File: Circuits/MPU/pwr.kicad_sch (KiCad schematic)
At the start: 0 parts

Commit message: more transcription
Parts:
- added 	U1: ProASIC, Package_BGA:BGA-484_23.0x23.0mm_Layout22x22_P1.0mm, symbol QuERI_FPGA:ProASIC
- added C100, C101, C102, C103, C104, C105, C106, C99: 22nF, Capacitor_SMD:C_0603_1608Metric, symbol QuERI_symbols:Csmall
- added C107, C108, C109, C110, C111: 0.1uF, Capacitor_SMD:C_0805_2012Metric, symbol QuERI_symbols:C
- added C112, C113: 0.1uF, Capacitor_SMD:C_0603_1608Metric, symbol QuERI_symbols:Csmall
- added C114: 10uF, Capacitor_SMD:C_0805_2012Metric, symbol QuERI_symbols:C
- added C115, C116, C80: DNP, Capacitor_SMD:C_1210_3225Metric, symbol QuERI_symbols:C
- added C117, C79: 10uF, Capacitor_SMD:C_1210_3225Metric, symbol QuERI_symbols:C
- added C118, C120, C121, C123, C124, C129, C130, C131, C132: 1uF, Capacitor_SMD:C_0805_2012Metric, symbol QuERI_symbols:C
- added C119, C122: 7.5nF, Capacitor_SMD:C_0603_1608Metric, symbol QuERI_symbols:Csmall
- added C125, C127: 10nF, Capacitor_SMD:C_0603_1608Metric, symbol QuERI_symbols:Csmall
- added C126, C128: 47uF, Capacitor_SMD:C_1210_3225Metric, symbol QuERI_symbols:C
- added C73, C76, C78: 22uF, Capacitor_SMD:C_1210_3225Metric, symbol QuERI_symbols:C
- added C74, C75, C77: TBD, Capacitor_SMD:C_1210_3225Metric, symbol QuERI_symbols:C
- added D10, D11, D12, D13, D14, D15, D16, D17, D18, D19, D20, D21, D9: 1N914UR, Diode_SMD:D_MiniMELF, symbol QuERI_symbols:1N914UR
- added L1, L2, L3, L4, L7: 4.7uH, Inductor_SMD:L_1008_2520Metric, symbol Device:L
- added PS1: JCA0624S03, symbol QuERI_symbols:JCA0624S03
- added PS2: JCE0324D05, symbol QuERI_symbols:JCE0324D05
- added Q7, Q8: MMBT2222A, Package_TO_SOT_SMD:SOT-23, symbol Transistor_BJT:MMBT2222A
- added R155, R156, R157, R158, R159, R160: 169, Resistor_SMD:R_1206_3216Metric, symbol Device:R
- added R161, R163: 4.99k, Resistor_SMD:R_0603_1608Metric, symbol QuERI_symbols:Rlowp
- added R162, R180: 49.9, Resistor_SMD:R_0603_1608Metric, symbol QuERI_symbols:Rlowp
- added R164, R167: 3.01k, Resistor_SMD:R_0603_1608Metric, symbol QuERI_symbols:Rlowp
- added R165, R166, R171, R178: 1, Resistor_SMD:R_0603_1608Metric, symbol QuERI_symbols:Rlowp
- added R168, R173: 3.74k, Resistor_SMD:R_0603_1608Metric, symbol QuERI_symbols:Rlowp
- added R169, R174: 15.0k, Resistor_SMD:R_0603_1608Metric, symbol QuERI_symbols:Rlowp
- added R170: 1.87k, Resistor_SMD:R_0603_1608Metric, symbol QuERI_symbols:Rlowp
- added R172, R176, R177: 18.2k, Resistor_SMD:R_0603_1608Metric, symbol QuERI_symbols:Rlowp
- added R175, R179, R181: 4.99, Resistor_SMD:R_0603_1608Metric, symbol QuERI_symbols:Rlowp
- added T1: HPH1-1400L, symbol QuERI_symbols:Hexapath
- added U26: DG403, Package_SO:SOIC-16_3.9x9.9mm_P1.27mm, symbol QuERI_symbols:DG403
- added U27: REF43GS, Package_SO:SOIC-8_3.9x4.9mm_P1.27mm, symbol QuERI_symbols:REF43GS
- added U28, U29: ADA4805-2ARMZ, Package_SO:MSOP-8_3x3mm_P0.65mm, symbol QuERI_symbols:ADA4805-2ARMZ
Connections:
- net +3.3raw: now also C74.1, L1.1, PS1.14 (+Vout)
- net +5raw: now also C75.1, L2.1, PS2.14 (+Vout)
- net -5raw: now also C77.1, L3.1, PS2.11 (-Vout)
- new net: C107.1, C109.2, D10.2 (A), D11.1 (K)
- new net: C106.1, C108.2, D11.2 (A), D12.1 (K)
- new net: C112.1, R155.2, U26.11 (V+), U26.12 (VL)
- new net: C123.1, R168.2, R169.2, U28.5 (+)
- new net: R160.2, U26.9 (S2)
- new net: C131.1, R180.2, U29.8 (V+)
- new net: Q8.1 (B), U29.1
- new net: C127.2, R177.1, U29.2 (-)
- new net: R176.2, U29.3 (+)
- new net: C101.2, C99.1, D18.2 (A), D19.1 (K)
- new net: C105.1, C107.2, D12.2 (A), D13.1 (K)
- new net: C103.1, C105.2, D14.2 (A), D15.1 (K)
- new net: C119.2, R163.2, R164.1, U28.2 (-)
- new net: C104.1, C106.2, D13.2 (A), D14.1 (K)
- new net: C102.1, C104.2, D15.2 (A), D16.1 (K)
- new net: C118.1, R162.2, U27.2 (VIN)
- new net: C125.1, Q7.2 (E), R171.1
- new net: C125.2, R172.1, U29.6 (-)
- new net: R173.2, R174.2, U29.5 (+)
- new net: C117.1, C79.2, L7.2, PS1.2 (-Vin), PS1.3 (-Vin), PS2.2 (-Vin), PS2.3 (-Vin)
- new net: C117.2, C79.1, L4.2, PS1.22 (+Vin), PS1.23 (+Vin), PS2.22 (+Vin), PS2.23 (+Vin)
- new net: C101.1, C103.2, D16.2 (A), D17.1 (K)
- new net: C100.1, C102.2, D17.2 (A), D18.1 (K)
- new net: C108.1, C110.2, D10.1 (K), D9.2 (A)
- new net: C127.1, Q8.2 (E), R178.1
- new net: C132.1, R181.2, U28.8 (V+)
- new net: Q7.1 (B), U29.7
- new net: C129.1, Q8.3 (C), R179.2
- new net: R159.2, U26.5 (S4)
- new net: C110.1, T1.9
- new net: R158.2, U26.16 (S1)
- new net: C100.2, D19.2 (A), D20.1 (K)
- new net: C130.1, Q7.3 (C), R175.2
- new net: C119.1, R165.1, U28.1
- new net: C124.1, R170.2, U28.3 (+)
- new net: C111.1, U26.1 (D1), U26.3 (D3), U26.6 (D4), U26.8 (D2)
- new net: C111.2, T1.2, T1.6
- new net: 	U1.AB12 (PUR), C114.1, D21.2 (A), R161.2
- new net: 	U1.AB13 (HVCLK), U26.10 (IN2), U26.15 (IN1)
- new net: C122.2, R167.1, U28.6 (-)
- new net: C122.1, R166.1, U28.7
- new net: C113.1, R156.2, U26.14 (V-)
- new net: R157.2, U26.4 (S3)
- new net: T1.1, T1.5
- new net: T1.10, T1.3
- new net: T1.11, T1.7
- new net: T1.12, T1.8
- new net +1.5V: C126.1, R171.2, R172.2
- new net +2.5F: C128.1, R177.2, R178.2
- new net +2.5V: R168.1, R170.1, R173.1, R176.1, U27.6 (VOUT)
- new net +28V: C116.2, C80.1, L4.1
- new net +28return: C115.1, C80.2, L7.1
- new net +3.3V: C73.1, D21.1 (K), L1.2, R161.1, R175.1, R179.1
- new net +5V: C76.1, L2.2, R155.1, R158.1, R160.1, R162.1, R180.1, R181.1
- new net -5V: C78.1, L3.2, R156.1, R157.1, R159.1
- new net -HVunreg: C99.2, D20.2 (A)
- new net GND: C109.1, C112.2, C113.2, C114.2, C115.2, C116.1, C118.2, C120.2, C121.2, C123.2, C124.2, C126.2, C128.2, C129.2, C130.2, C131.2, C132.2, C73.2, C74.2, C75.2, C76.2, C77.2, C78.2, D9.1 (K), PS1.16 (-Vout), PS2.16 (0V), PS2.9 (0V), R163.1, R169.1, R174.1, T1.4, U26.13 (GND), U27.4 (GND), U28.4 (V-), U29.4 (V-)
- new net VFS: C120.1, R164.2, R165.2
- new net VHS: C121.1, R166.2, R167.2

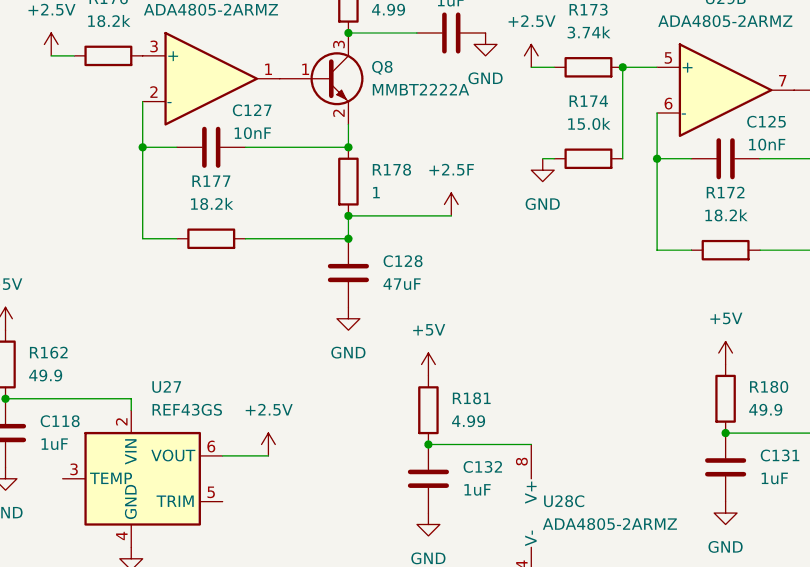
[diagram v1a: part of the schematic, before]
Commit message: All pages populated with parts
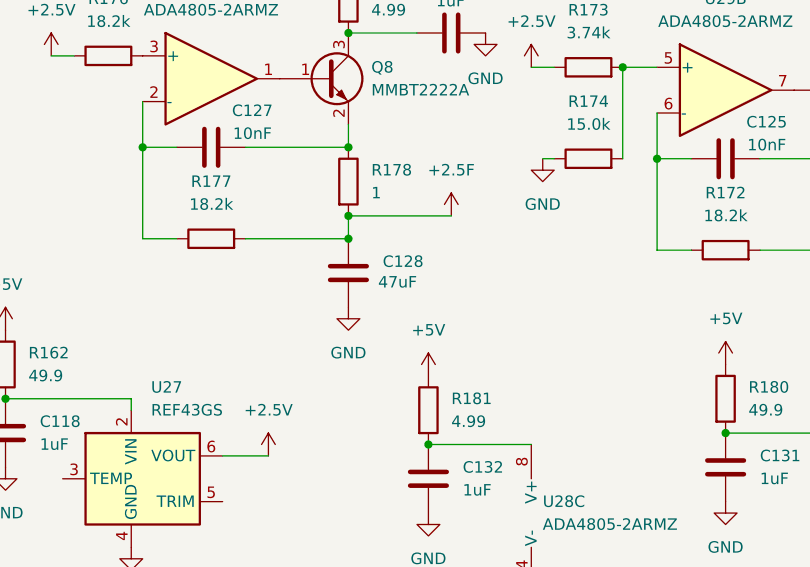
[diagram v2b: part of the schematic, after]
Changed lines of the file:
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@@
 		)
 		(property "Value" "47uF"
-			(at 195.58 130.8099 0)
+			(at 195.072 130.556 0)
 			(effects
 				(font

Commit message: Passes DRC
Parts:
- removed 	U1: ProASIC, Package_BGA:BGA-484_23.0x23.0mm_Layout22x22_P1.0mm, symbol QuERI_FPGA:ProASIC
- added U1: ProASIC, Package_BGA:BGA-484_23.0x23.0mm_Layout22x22_P1.0mm, symbol QuERI_FPGA:ProASIC
- C37: renamed from C114; Spec 10WVDC X7R -> 16WVDC X7R
- C38: renamed from C116; Spec 50WVDC X7S -> 16WVDC X7R
- C39: renamed from C115; Spec 50WVDC X7S -> 16WVDC X7R
- C40: renamed from C80; Spec 50WVDC X7S -> 16WVDC X7R
- C41: renamed from C79; Spec 50WVDC X7S -> 16WVDC X7R
- C42: renamed from C117; Spec 50WVDC X7S -> 16WVDC X7R
- C43: renamed from C112; Spec 10WVDC X7R -> 50WVDC C0G
- C44: renamed from C113; Spec 10WVDC X7R -> 50WVDC C0G
- C45: renamed from C111; Spec 50WVDC X7R -> 16WVDC X7R
- C52: renamed from C110; Spec 50WVDC X7R -> 16WVDC X7R
- C53: renamed from C109; Spec 50WVDC X7R -> 16WVDC X7R
- C55: renamed from C108; Spec 50WVDC X7R -> 16WVDC X7R
- C57: renamed from C107; Spec 50WVDC X7R -> 16WVDC X7R
- C58: renamed from C127; Spec 10WVDC X7R -> 50WVDC C0G
- C59: renamed from C106; Spec 50WVDC X7R -> 50WVDC C0G
- C60: renamed from C119; Spec 10WVDC X7R -> 50WVDC C0G
- C61: renamed from C105; Spec 50WVDC X7R -> 50WVDC C0G
- C62: renamed from C128; Spec 6.3WVDC X7R -> 16WVDC X7R
- C63: renamed from C104; Spec 50WVDC X7R -> 50WVDC C0G
- C67: renamed from C103; Spec 50WVDC X7R -> 50WVDC C0G
- C68: renamed from C102; Spec 50WVDC X7R -> 50WVDC C0G
- C70: renamed from C101; Spec 50WVDC X7R -> 50WVDC C0G
- C71: renamed from C125; Spec 10WVDC X7R -> 50WVDC C0G
- C73: renamed from C122; Spec 10WVDC X7R -> 50WVDC C0G
- C74: renamed from C100; Spec 50WVDC X7R -> 50WVDC C0G
- C75: renamed from C126; Spec 6.3WVDC X7R -> 16WVDC X7R
- C76: renamed from C99; Spec 50WVDC X7R -> 50WVDC C0G
- renumbered C74 to C46, C75 to C47, C77 to C48, C73 to C49, C76 to C50, C78 to C51, C118 to C54, C124 to C56, C132 to C64, C120 to C65, C129 to C66, C123 to C69, C131 to C72, C121 to C77, C130 to C78, D16 to D10, D17 to D11, D18 to D12, D19 to D13, D20 to D14, D21 to D2, D9 to D3, D10 to D4, D11 to D5, D12 to D6, D13 to D7, D14 to D8, D15 to D9, L4 to L3, L7 to L4, L1 to L5, L2 to L6, L3 to L7, Q8 to Q7, Q7 to Q8, R166 to R100, R161 to R74, R157 to R75, R158 to R76, R159 to R77, R160 to R78, R155 to R79, R156 to R80, R162 to R81, R170 to R82, R176 to R83, R163 to R84, R177 to R85, R164 to R86, R179 to R87, R178 to R88, R165 to R89, R181 to R90, R173 to R91, R174 to R92, R168 to R93, R169 to R94, R172 to R95, R180 to R96, R167 to R97, R175 to R98, R171 to R99, U26 to U16, U27 to U17, U29 to U18, U28 to U18, U29 to U19, U28 to U19
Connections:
- net ~{PUR}: now reaches C37.1, D2.2 (A), R74.2
- net ~{PUR}: now also U1.AB12 (PUR)
- net HVCLK: now reaches U16.10 (IN2), U16.15 (IN1)
- net HVCLK: now also U1.AB13 (HVCLK)
- no-connect marks 0 -> 2

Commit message: bunch of little fixes
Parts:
- C37: Spec 16WVDC X7R -> 10WVDC X7R
- C38, C39, C40: value DNP -> 10uF; Spec 16WVDC X7R -> 50WVDC X7R; now not fitted
- C41, C42: Spec 16WVDC X7R -> 50WVDC X7R
- C43, C44, C59, C61, C63, C67, C68, C70, C74, C76: Spec 50WVDC C0G -> 50WVDC X7R
- C45, C52, C53, C55, C57: footprint Capacitor_SMD:C_0805_2012Metric -> Capacitor_SMD:C_0603_1608Metric; Spec 16WVDC X7R -> 50WVDC X7R
- C62, C75: Spec 16WVDC X7R -> 6.3WVDC X7R
- PS1, PS2: footprint (none) -> Package_DIP:DIP-24_W15.24mm_Socket
- U1: footprint Package_BGA:BGA-484_23.0x23.0mm_Layout22x22_P1.0mm -> Package_BGA:BGA-484_23.0x23.0mm_Layout22x22_P1.0mm
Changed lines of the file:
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@@
 	(title_block
 		(title "QuERI MPU")
-		(date "2024-03-28")
+		(date "2024-05-26")
 		(rev "Draft")
 		(company "Noqsi Aerospace Ltd")
@@
 			)
 		)
-		(property "Footprint" "	Package_BGA:BGA-484_23.0x23.0mm_Layout22x22_P1.0mm"
+		(property "Footprint" "Package_BGA:BGA-484_23.0x23.0mm_Layout22x22_P1.0mm"
 			(at 30.48 69.85 0)
 			(effects
@@
 			)
 		)
-		(property "Spec" "50WVDC C0G"
+		(property "Spec" "50WVDC X7R"
 			(at 251.46 26.67 0)
 			(effects
@@
 			)
 		)
-		(property "Spec" "50WVDC C0G"
+		(property "Spec" "50WVDC X7R"
 			(at 190.5 26.67 0)
 			(effects
@@
 		(in_bom yes)
 		(on_board yes)
-		(dnp no)
+		(dnp yes)
 		(fields_autoplaced yes)
 		(property "Reference" "C39"
@@
 			)
 		)
-		(property "Value" "DNP"
+		(property "Value" "10uF"
 			(at 44.45 160.0199 0)
 			(effects
@@
 			)
 		)
-		(property "Spec" "16WVDC X7R"
+		(property "Spec" "50WVDC X7R"
 			(at 40.64 158.75 0)
 			(effects
@@
 			)
 		)
-		(property "Spec" "50WVDC C0G"
+		(property "Spec" "50WVDC X7R"
 			(at 200.66 48.26 0)
 			(effects
@@
 			)
 		)
-		(property "Footprint" ""
+		(property "Footprint" "Package_DIP:DIP-24_W15.24mm_Socket"
 			(at 59.69 175.26 0)
 			(effects
@@
 			)
 		)
-		(property "Spec" "50WVDC C0G"
+		(property "Spec" "50WVDC X7R"
 			(at 210.82 26.67 0)
 			(effects
@@
 			)
 		)
-		(property "Spec" "50WVDC C0G"
+		(property "Spec" "50WVDC X7R"
 			(at 220.98 48.26 0)
 			(effects
@@
 			)
 		)
-		(property "Footprint" "Capacitor_SMD:C_0805_2012Metric"
+		(property "Footprint" "Capacitor_SMD:C_0603_1608Metric"
 			(at 173.99 25.7048 0)
 			(effects
@@
 			)
 		)
-		(property "Spec" "16WVDC X7R"
+		(property "Spec" "50WVDC X7R"
 			(at 170.18 26.67 0)
 			(effects
@@
 			)
 		)
-		(property "Spec" "16WVDC X7R"
+		(property "Spec" "50WVDC X7R"
 			(at 64.77 135.89 0)
 			(effects
@@
 			)
 		)
-		(property "Spec" "16WVDC X7R"
+		(property "Spec" "6.3WVDC X7R"
 			(at 191.77 129.54 0)
 			(effects
@@
 			)
 		)
-		(property "Footprint" "Capacitor_SMD:C_0805_2012Metric"
+		(property "Footprint" "Capacitor_SMD:C_0603_1608Metric"
 			(at 143.51 47.2948 0)
 			(effects
@@
 			)
 		)
-		(property "Spec" "16WVDC X7R"
+		(property "Spec" "50WVDC X7R"
 			(at 139.7 48.26 0)
 			(effects
@@
 			)
 		)
-		(property "Footprint" "Capacitor_SMD:C_0805_2012Metric"
+		(property "Footprint" "Capacitor_SMD:C_0603_1608Metric"
 			(at 109.22 70.1548 0)
 			(effects
@@
 			)
 		)
-		(property "Spec" "16WVDC X7R"
+		(property "Spec" "50WVDC X7R"
 			(at 105.41 71.12 0)
 			(effects
@@
 			)
 		)
-		(property "Footprint" "Capacitor_SMD:C_0805_2012Metric"
+		(property "Footprint" "Capacitor_SMD:C_0603_1608Metric"
 			(at 153.67 25.7048 0)
 			(effects
@@
 			)
 		)
-		(property "Spec" "16WVDC X7R"
+		(property "Spec" "50WVDC X7R"
 			(at 149.86 26.67 0)
 			(effects
@@
 			)
 		)
-		(property "Spec" "16WVDC X7R"
+		(property "Spec" "50WVDC X7R"
 			(at 66.04 163.83 0)
 			(effects
@@
 			)
 		)
-		(property "Spec" "50WVDC C0G"
+		(property "Spec" "50WVDC X7R"
 			(at 231.14 26.67 0)
 			(effects
@@
 			)
 		)
-		(property "Spec" "50WVDC C0G"
+		(property "Spec" "50WVDC X7R"
 			(at 180.34 48.26 0)
 			(effects
@@
 			)
 		)
-		(property "Spec" "16WVDC X7R"
+		(property "Spec" "10WVDC X7R"
 			(at 36.83 105.41 0)
 			(effects
@@
 			)
 		)
-		(property "Spec" "16WVDC X7R"
+		(property "Spec" "6.3WVDC X7R"
 			(at 248.92 130.81 0)
 			(effects
@@
 			)
 		)
-		(property "Spec" "50WVDC C0G"
+		(property "Spec" "50WVDC X7R"
 			(at 71.12 43.18 0)
 			(effects
@@
 		(in_bom yes)
 		(on_board yes)
-		(dnp no)
+		(dnp yes)
 		(fields_autoplaced yes)
 		(property "Reference" "C38"
@@
 			)
 		)
-		(property "Value" "DNP"
+		(property "Value" "10uF"
 			(at 44.45 135.8899 0)
 			(effects
@@
 			)
 		)
-		(property "Spec" "16WVDC X7R"
+		(property "Spec" "50WVDC X7R"
 			(at 40.64 134.62 0)
 			(effects
@@
 		(in_bom yes)
 		(on_board yes)
-		(dnp no)
+		(dnp yes)
 		(fields_autoplaced yes)
 		(property "Reference" "C40"
@@
 			)
 		)
-		(property "Value" "DNP"
+		(property "Value" "10uF"
 			(at 48.26 146.0499 0)
 			(effects
@@
 			)
 		)
-		(property "Spec" "16WVDC X7R"
+		(property "Spec" "50WVDC X7R"
 			(at 44.45 144.78 0)
 			(effects
@@
 			)
 		)
-		(property "Footprint" "Capacitor_SMD:C_0805_2012Metric"
+		(property "Footprint" "Capacitor_SMD:C_0603_1608Metric"
 			(at 163.83 47.2948 0)
 			(effects
@@
 			)
 		)
-		(property "Spec" "16WVDC X7R"
+		(property "Spec" "50WVDC X7R"
 			(at 160.02 48.26 0)
 			(effects
@@
 			)
 		)
-		(property "Spec" "50WVDC C0G"
+		(property "Spec" "50WVDC X7R"
 			(at 72.39 95.25 0)
 			(effects
@@
 			)
 		)
-		(property "Footprint" ""
+		(property "Footprint" "Package_DIP:DIP-24_W15.24mm_Socket"
 			(at 59.69 137.16 0)
 			(effects
@@
 			)
 		)
-		(property "Spec" "50WVDC C0G"
+		(property "Spec" "50WVDC X7R"
 			(at 241.3 48.26 0)
 			(effects
